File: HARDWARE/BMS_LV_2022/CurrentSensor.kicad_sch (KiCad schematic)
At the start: 5 parts, among them U5 ACHS-7123

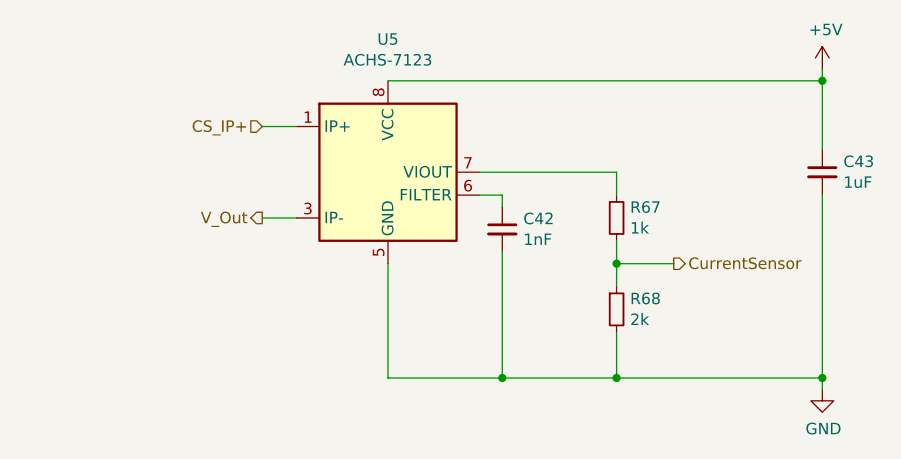
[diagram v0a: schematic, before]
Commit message: New fuses and programming connector added
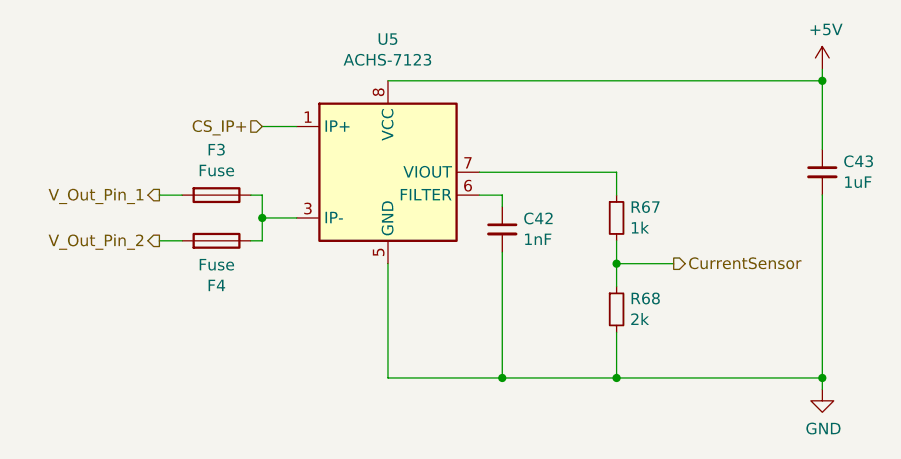
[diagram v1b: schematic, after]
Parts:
- added F3, F4: Fuse, footprints:0154001.DRT, symbol Device:Fuse
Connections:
- net V_Out: no longer names the net of U5.3 (IP-), U5.4 (IP-)
- net V_Out: now also F3.1, F4.1
- new net V_Out_Pin_1: F3.2
- new net V_Out_Pin_2: F4.2
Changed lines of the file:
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@@
+	)
+	(junction
+		(at 123.19 99.06)
+		(diameter 0)
+		(color 0 0 0 0)
 	)
 	(junction
@@
 	(wire
 		(pts
+			(xy 127 99.06) (xy 123.19 99.06)
+		)
+		(stroke
+			(width 0)
+			(type default)
+		)
+	)
+	(wire
+		(pts
 			(xy 162.56 93.98) (xy 162.56 96.52)
 		)
@@
 	(wire
 		(pts
+			(xy 123.19 101.6) (xy 121.92 101.6)
+		)
+		(stroke
+			(width 0)
+			(type default)
+		)
+	)
+	(wire
+		(pts
 			(xy 162.56 104.14) (xy 162.56 106.68)
 		)
@@
 	(wire
 		(pts
+			(xy 123.19 99.06) (xy 123.19 101.6)
+		)
+		(stroke
+			(width 0)
+			(type default)
+		)
+	)
+	(wire
+		(pts
+			(xy 123.19 96.52) (xy 121.92 96.52)
+		)
+		(stroke
+			(width 0)
+			(type default)
+		)
+	)
+	(wire
+		(pts
 			(xy 162.56 101.6) (xy 162.56 104.14)
 		)
@@
 	(wire
 		(pts
+			(xy 123.19 99.06) (xy 123.19 96.52)
+		)
+		(stroke
+			(width 0)
+			(type default)
+		)
+	)
+	(wire
+		(pts
 			(xy 149.86 96.52) (xy 149.86 97.79)
 		)
@@
 	(wire
 		(pts
+			(xy 111.76 101.6) (xy 114.3 101.6)
+		)
+		(stroke
+			(width 0)
+			(type default)
+		)
+	)
+	(wire
+		(pts
+			(xy 111.76 96.52) (xy 114.3 96.52)
+		)
+		(stroke
+			(width 0)
+			(type default)
+		)
+	)
+	(wire
+		(pts
 			(xy 147.32 93.98) (xy 162.56 93.98)
 		)
@@
 		(pts
 			(xy 127 88.9) (xy 123.19 88.9)
-		)
-		(stroke
-			(width 0)
-			(type default)
-		)
-	)
-	(wire
-		(pts
-			(xy 127 99.06) (xy 123.19 99.06)
 		)
 		(stroke
@@
 		(shape input)
 		(at 123.19 88.9 180)
+		(fields_autoplaced yes)
 		(effects
 			(font
@@
 		(shape output)
 		(at 168.91 104.14 0)
+		(fields_autoplaced yes)
 		(effects
 			(font
@@
 		)
 	)
-	(hierarchical_label "V_Out"
+	(hierarchical_label "V_Out_Pin_2"
 		(shape output)
-		(at 123.19 99.06 180)
+		(at 111.76 101.6 180)
+		(fields_autoplaced yes)
+		(effects
+			(font
+				(size 1.27 1.27)
+			)
+			(justify right)
+		)
+	)
+	(hierarchical_label "V_Out_Pin_1"
+		(shape output)
+		(at 111.76 96.52 180)
+		(fields_autoplaced yes)
 		(effects
 			(font
@@
 					(unit 1)
 				)
-				(path "/fb6504b5-591d-4b10-ab86-0c46f59e8b7d"
-					(reference "U?")
-					(unit 1)
-				)
 			)
 		)
@@
 					(unit 1)
 				)
-				(path "/fb6504b5-591d-4b10-ab86-0c46f59e8b7d"
-					(reference "C?")
-					(unit 1)
-				)
 			)
 		)
@@
 					(unit 1)
 				)
-				(path "/fb6504b5-591d-4b10-ab86-0c46f59e8b7d"
-					(reference "C?")
-					(unit 1)
-				)
 			)
 		)
@@
 					(unit 1)
 				)
-				(path "/fb6504b5-591d-4b10-ab86-0c46f59e8b7d"
-					(reference "#PWR?")
-					(unit 1)
-				)
 			)
 		)
@@
 					(unit 1)
 				)
-				(path "/fb6504b5-591d-4b10-ab86-0c46f59e8b7d"
-					(reference "#PWR?")
+			)
+		)
+	)
+	(symbol
+		(lib_id "Device:Fuse")
+		(at 118.11 96.52 270)
+		(unit 1)
+		(exclude_from_sim no)
+		(in_bom yes)
+		(on_board yes)
+		(dnp no)
+		(property "Reference" "F3"
+			(at 118.11 91.5162 90)
+			(effects
+				(font
+					(size 1.27 1.27)
+				)
+			)
+		)
+		(property "Value" "Fuse"
+			(at 118.11 93.8276 90)
+			(effects
+				(font
+					(size 1.27 1.27)
+				)
+			)
+		)
+		(property "Footprint" "footprints:0154001.DRT"
+			(at 118.11 94.742 90)
+			(effects
+				(font
+					(size 1.27 1.27)
+				)
+				(hide yes)
+			)
+		)
+		(property "Datasheet" "http://m.littelfuse.com/~/media/electronics/datasheets/fuses/littelfuse_fuse_154_154t_154l_154tl_datasheet.pdf.pdf"
+			(at 118.11 96.52 0)
+			(effects
+				(font
+					(size 1.27 1.27)
+				)
+				(hide yes)
+			)
+		)
+		(property "Description" ""
+			(at 118.11 96.52 0)
+			(effects
+				(font
+					(size 1.27 1.27)
+				)
+				(hide yes)
+			)
+		)
+		(property "Part Number" "0154010.DR"
+			(at 118.11 96.52 0)
+			(effects
+				(font
+					(size 1.27 1.27)
+				)
+				(hide yes)
+			)
+		)
+		(pin "2"
+		)
+		(pin "1"
+		)
+		(instances
+			(project "BMS_LV_2022"
+				(path "/fb6504b5-591d-4b10-ab86-0c46f59e8b7d/00000000-0000-0000-0000-000062c2dd72"
+					(reference "F3")
 					(unit 1)
 				)
+			)
+		)
+	)
+	(symbol
+		(lib_id "Device:Fuse")
+		(at 118.11 101.6 270)
+		(mirror x)
+		(unit 1)
+		(exclude_from_sim no)
+		(in_bom yes)
+		(on_board yes)
+		(dnp no)
+		(property "Reference" "F4"
+			(at 118.11 106.6038 90)
+			(effects
+				(font
+					(size 1.27 1.27)
+				)
+			)
+		)
+		(property "Value" "Fuse"
+			(at 118.11 104.2924 90)
+			(effects
+				(font
+					(size 1.27 1.27)
+				)
+			)
+		)
+		(property "Footprint" "footprints:0154001.DRT"
+			(at 118.11 103.378 90)
+			(effects
+				(font
+					(size 1.27 1.27)
+				)
+				(hide yes)
+			)
+		)
+		(property "Datasheet" "http://m.littelfuse.com/~/media/electronics/datasheets/fuses/littelfuse_fuse_154_154t_154l_154tl_datasheet.pdf.pdf"
+			(at 118.11 101.6 0)
+			(effects
+				(font
+					(size 1.27 1.27)
+				)
+				(hide yes)
+			)
+		)
+		(property "Description" ""
+			(at 118.11 101.6 0)
+			(effects
+				(font
+					(size 1.27 1.27)
+				)
+				(hide yes)
+			)
+		)
+		(property "Part Number" "0154010.DR"
+			(at 118.11 101.6 0)
+			(effects
+				(font
+					(size 1.27 1.27)
+				)
+				(hide yes)
+			)
+		)
+		(pin "2"
+		)
+		(pin "1"
+		)
+		(instances
+			(project "BMS_LV_2022"
+				(path "/fb6504b5-591d-4b10-ab86-0c46f59e8b7d/00000000-0000-0000-0000-000062c2dd72"
+					(reference "F4")
+					(unit 1)
+				)
